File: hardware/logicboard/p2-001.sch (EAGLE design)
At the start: 54 parts, among them IC1 5V, IC2 4066N, IC3 LTC485N, IC4 74LS07N, J1 LEDs, J2 Display, J3 PWR, K1 G5V1, Q1 220mA/50V/3.5Ω, Q2 220mA/50V/3.5Ω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

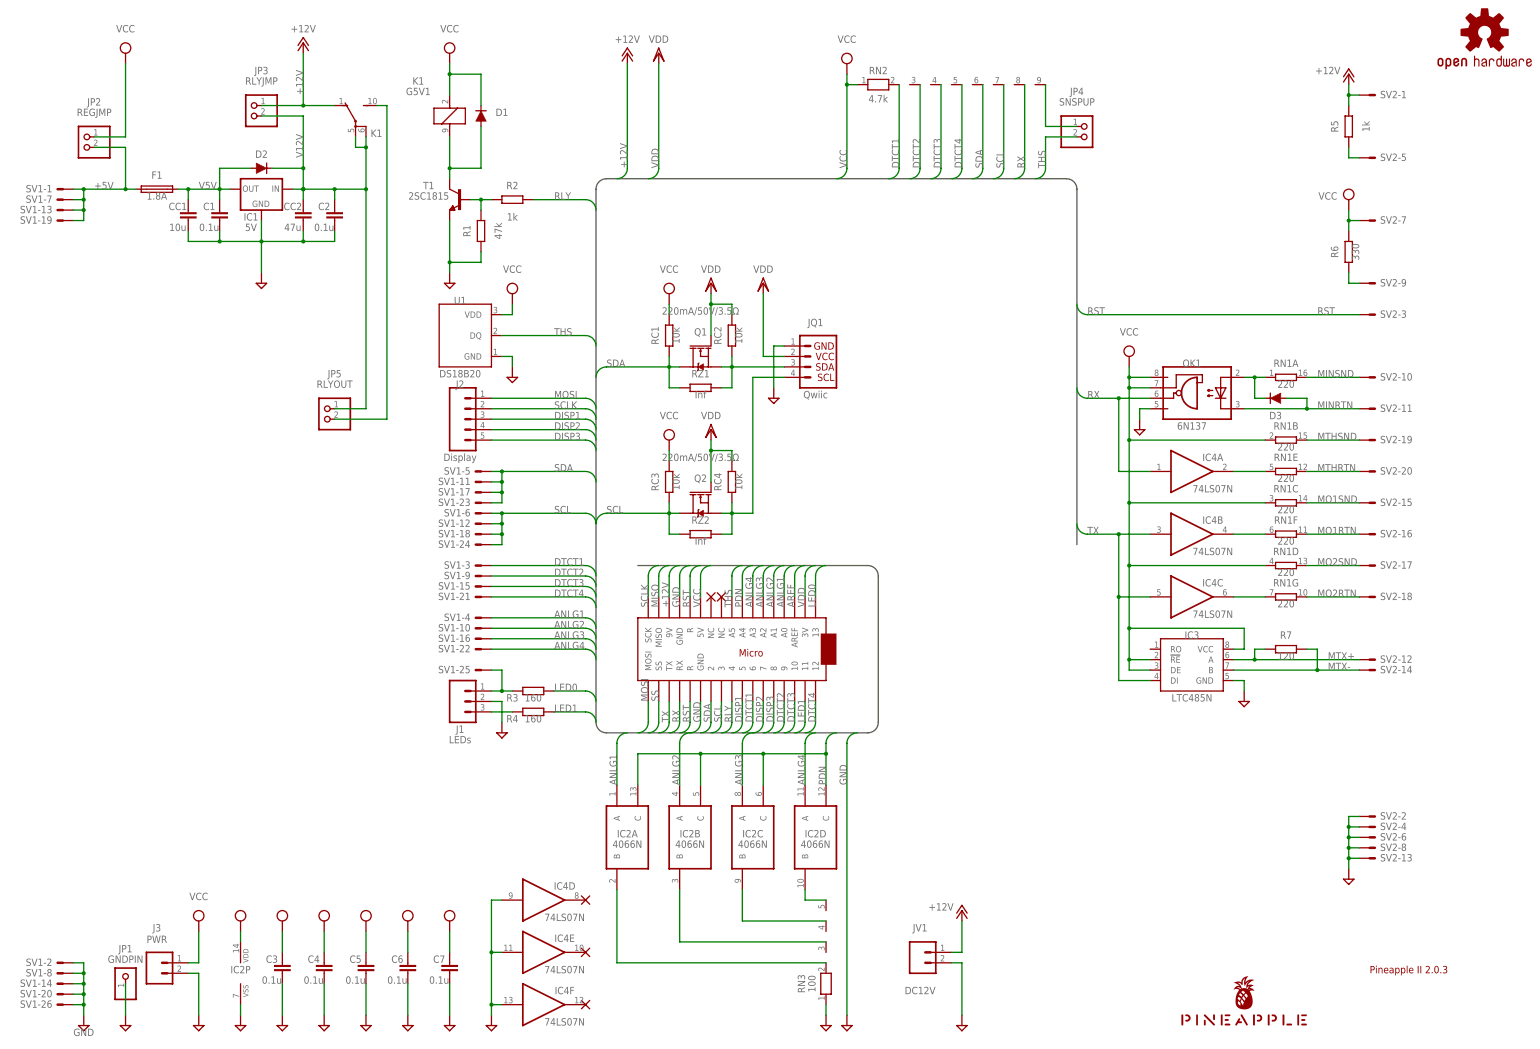
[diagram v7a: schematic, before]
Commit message: Now MIDI In+ has Aux pin.
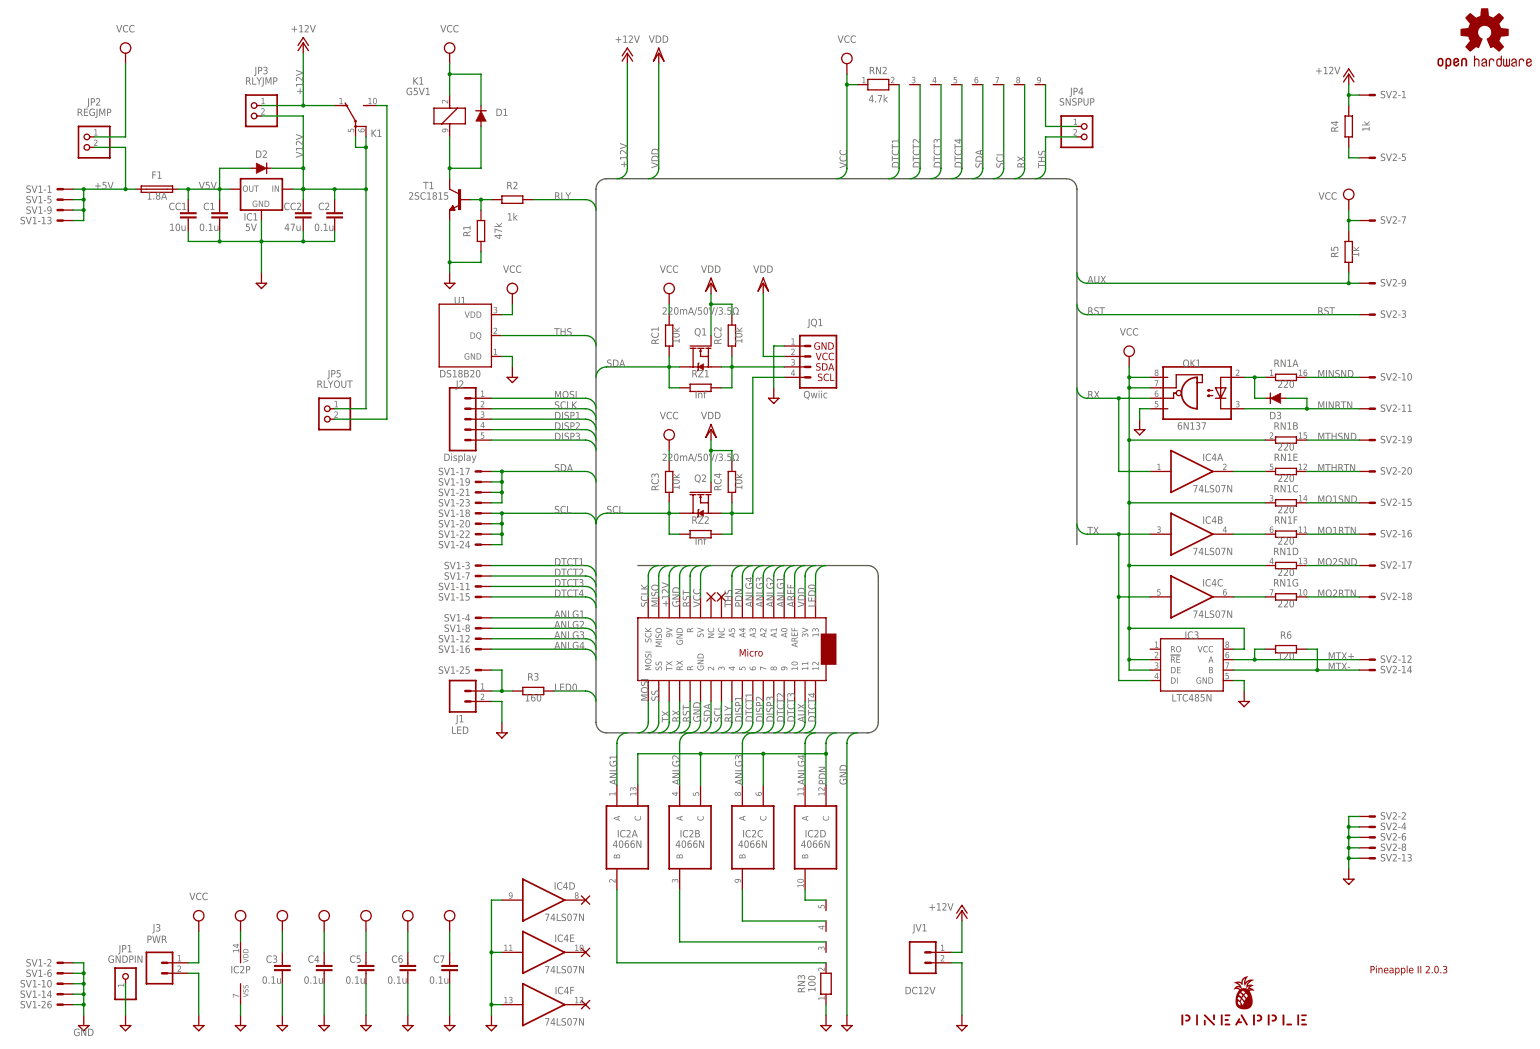
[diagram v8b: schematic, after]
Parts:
- removed R7: 120, resistor:R-EU_0204/5
- J1: value LEDs -> LED; device SparkFun-Connectors:CONN_03JST-PTH -> SparkFun-Connectors:CONN_02JST-PTH-2
- R4: value 160 -> 1k
- R6: value 330 -> 120
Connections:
- removed net LED1: MC1.11, R4.2
- removed net LED1A: J1.3, R4.1
- removed net N$1: R6.1, SV2-9.S
- new net AUX: MC1.11, R5.1, SV2-9.S
- net +12V: now also R4.2; no longer R5.2
- net +5V: now also SV1-5.S, SV1-9.S; no longer SV1-19.S, SV1-7.S
- net ANLG2: now also SV1-8.S; no longer SV1-10.S
- net ANLG3: now also SV1-12.S; no longer SV1-16.S
- net ANLG4: now also SV1-16.S; no longer SV1-22.S
- net DTCT2: now also SV1-7.S; no longer SV1-9.S
- net DTCT3: now also SV1-11.S; no longer SV1-15.S
- net DTCT4: now also SV1-15.S; no longer SV1-21.S
- net GND: now also SV1-10.S, SV1-6.S; no longer SV1-20.S, SV1-8.S
- net MTX+: now also R6.1; no longer R7.1
- net MTX-: now also R6.2; no longer R7.2
- net PWRLED: now also R4.1; no longer R5.1
- net SCL: now also SV1-20.S, SV1-22.S; no longer SV1-12.S, SV1-6.S
- net SDA: now also SV1-19.S, SV1-21.S; no longer SV1-11.S, SV1-5.S
- net VCC: now also R5.2; no longer R6.2
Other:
- moved on the sheet: R4, R5, R6, SV1-10, SV1-11, SV1-12, SV1-13, SV1-14, SV1-15, SV1-16, SV1-17, SV1-18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
